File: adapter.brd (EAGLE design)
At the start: 75.9 x 17.8 mm, 3 parts

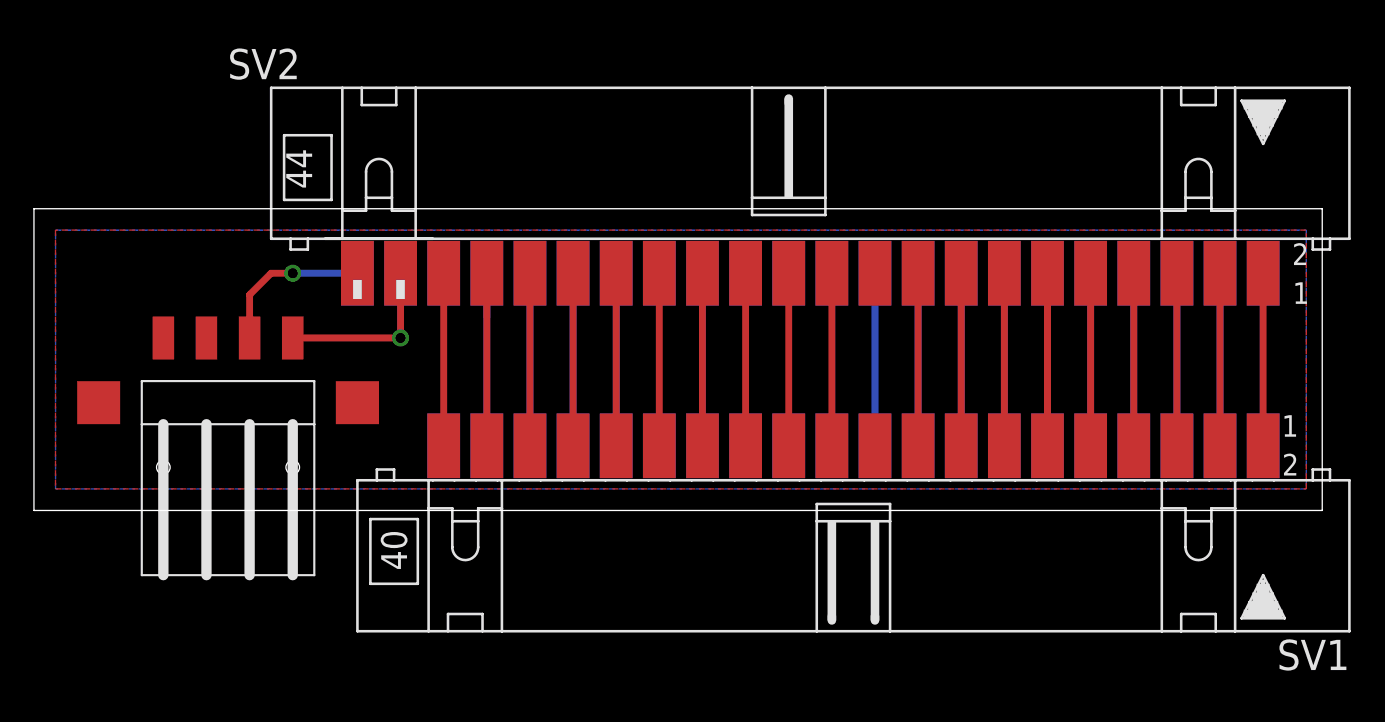
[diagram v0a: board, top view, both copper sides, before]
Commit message: Reduced pin pitch on the IDE 44 connector.
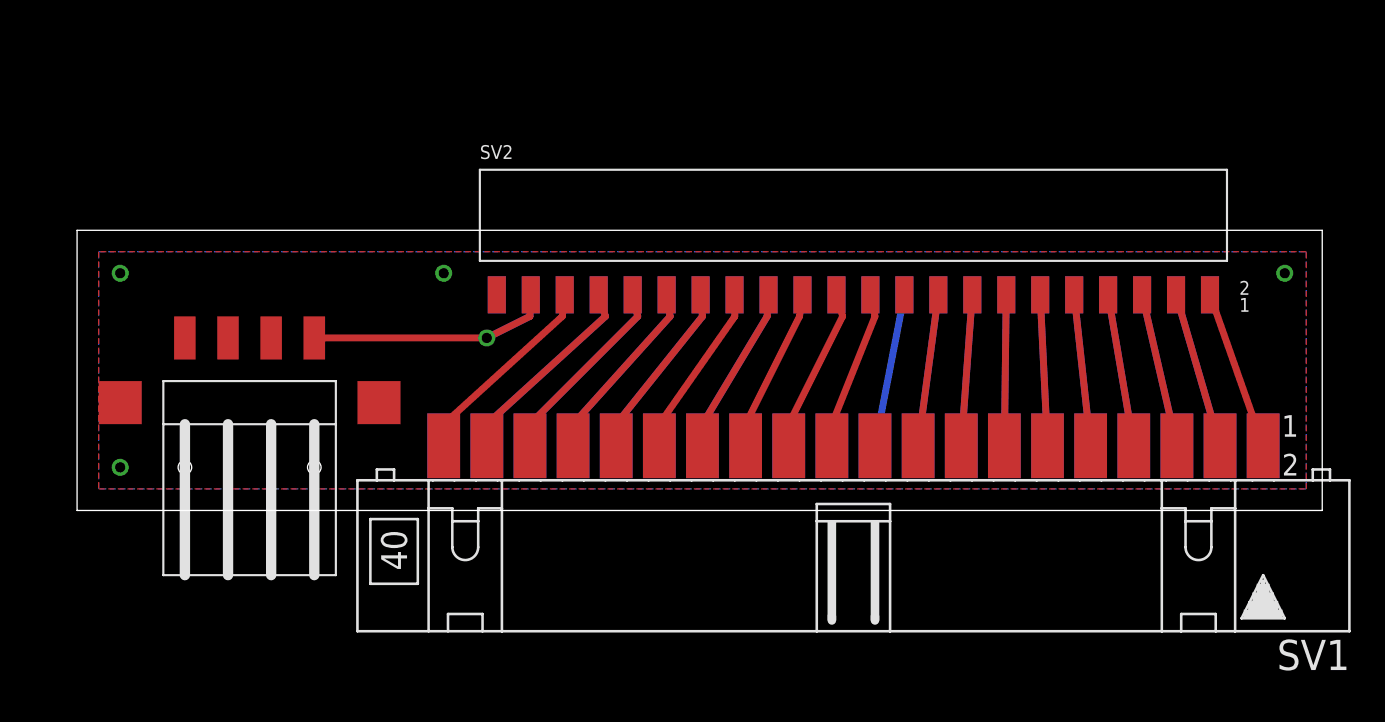
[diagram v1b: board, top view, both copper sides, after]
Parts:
- SV2: device conn:ML44SMDF -> conn:PINHEAD2X22F
- moved SV2 4.02 mm to (47.0, 11.4)
- moved U$1 1.27 mm to (11.4, 8.89)
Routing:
- net GND: track 9.42 -> 0.00 mm, vias 1 -> 4
- net N$3: track 14.0 -> 18.4 mm
- net IDE37: track 10.2 -> 12.0 mm
- net IDE39: track 10.2 -> 12.0 mm
- net IDE36: track 10.2 -> 11.6 mm
- net IDE35: track 10.2 -> 11.6 mm
- net IDE14: track 10.2 -> 8.89 mm
- net IDE13: track 10.2 -> 8.89 mm
- net IDE12: track 10.2 -> 8.90 mm
- net IDE11: track 10.2 -> 8.90 mm
- net IDE16: track 10.2 -> 8.91 mm
- net IDE15: track 10.2 -> 8.91 mm
- net IDE9: track 10.2 -> 8.94 mm
- net IDE10: track 10.2 -> 8.94 mm
- net IDE18: track 10.2 -> 8.97 mm
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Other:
- board size 75.9 x 17.8 mm -> 73.3 x 16.5 mm

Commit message: Added more space for the power plug.
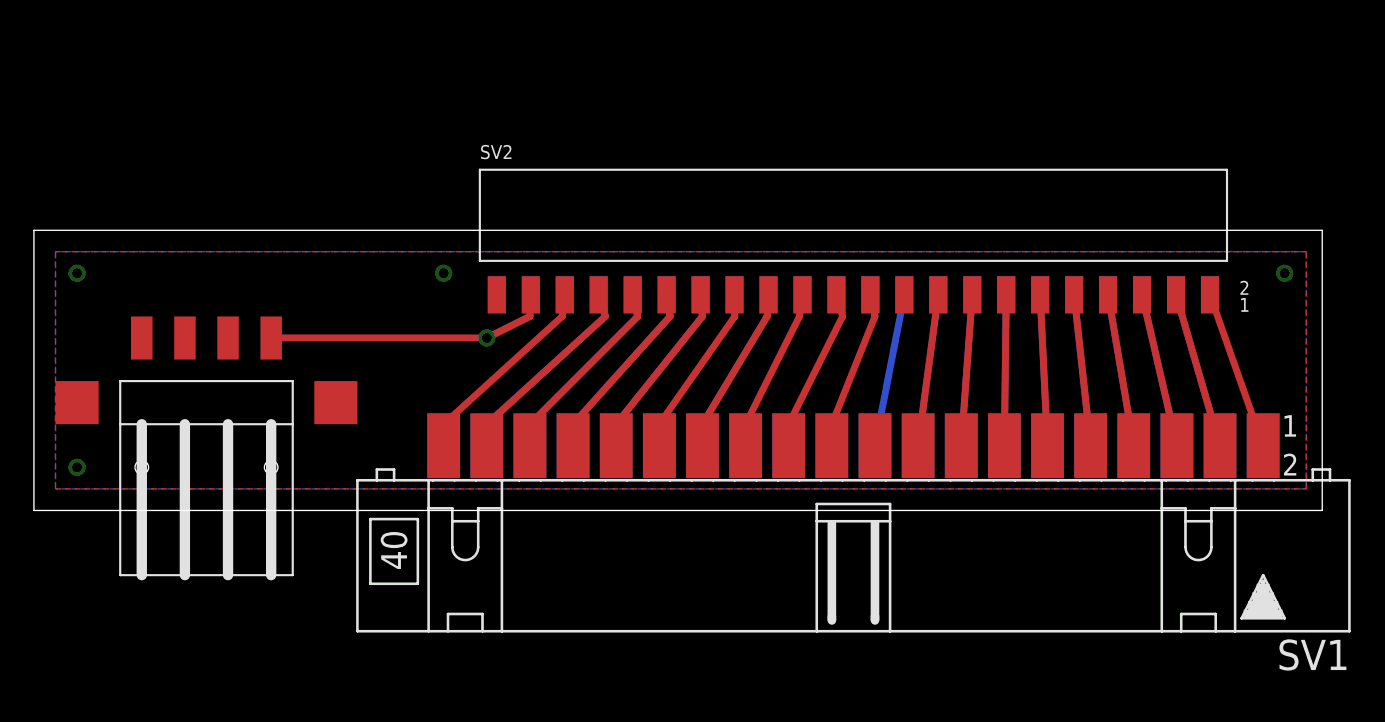
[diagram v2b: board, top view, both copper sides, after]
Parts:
- moved U$1 2.54 mm to (8.89, 8.89)
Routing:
- net N$3: track 18.4 -> 20.9 mm
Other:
- board size 73.3 x 16.5 mm -> 75.9 x 16.5 mm
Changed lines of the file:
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@@
 <board>
 <plain>
-<wire x1="1.27" y1="-1.27" x2="74.6" y2="-1.27" width="0" layer="20"/>
+<wire x1="-1.27" y1="-1.27" x2="74.6" y2="-1.27" width="0" layer="20"/>
 <wire x1="74.6" y1="-1.27" x2="74.6" y2="15.23" width="0" layer="20"/>
-<wire x1="74.6" y1="15.23" x2="1.27" y2="15.23" width="0" layer="20"/>
-<wire x1="1.27" y1="15.23" x2="1.27" y2="-1.27" width="0" layer="20"/>
+<wire x1="74.6" y1="15.23" x2="-1.27" y2="15.23" width="0" layer="20"/>
+<wire x1="-1.27" y1="15.23" x2="-1.27" y2="-1.27" width="0" layer="20"/>
 </plain>
 <attributes>
@@
 <element name="SV1" library="conn" package="ML40SMD" value="" x="46.99" y="2.54" rot="R180"/>
 <element name="SV2" library="conn" package="PINHEAD2X22F" value="" x="46.99" y="11.43"/>
-<element name="U$1" library="conn" package="FLOPPYPWR" value="FLOPPYPWR" x="11.43" y="8.89" rot="R180"/>
+<element name="U$1" library="conn" package="FLOPPYPWR" value="FLOPPYPWR" x="8.89" y="8.89" rot="R180"/>
 </elements>
 <signals>
@@
 <wire x1="27.94" y1="10.16" x2="25.4" y2="8.89" width="0.4064" layer="16"/>
 <via x="25.4" y="8.89" extent="1-16" drill="0.6" shape="square"/>
-<wire x1="25.4" y1="8.89" x2="15.24" y2="8.89" width="0.4064" layer="1"/>
+<wire x1="25.4" y1="8.89" x2="12.7" y2="8.89" width="0.4064" layer="1"/>
 </signal>
 <signal name="GND">
 <polygon width="0.4064" layer="1">
-<vertex x="2.54" y="0"/>
+<vertex x="0" y="0"/>
 <vertex x="73.66" y="0"/>
 <vertex x="73.66" y="13.97"/>
-<vertex x="2.54" y="13.97"/>
+<vertex x="0" y="13.97"/>
 </polygon>
 <polygon width="0.4064" layer="16">
-<vertex x="2.54" y="13.97"/>
+<vertex x="0" y="13.97"/>
 <vertex x="73.66" y="13.97"/>
 <vertex x="73.66" y="0"/>
-<vertex x="2.54" y="0"/>
+<vertex x="0" y="0"/>
 </polygon>
 <contactref element="U$1" pad="2"/>
@@
 <contactref element="SV1" pad="2"/>
 <contactref element="SV1" pad="19"/>
-<via x="3.81" y="12.7" extent="1-16" drill="0.6" shape="square"/>
+<via x="1.27" y="12.7" extent="1-16" drill="0.6" shape="square"/>
 <via x="22.86" y="12.7" extent="1-16" drill="0.6" shape="square"/>
-<via x="3.81" y="1.27" extent="1-16" drill="0.6" shape="square"/>
+<via x="1.27" y="1.27" extent="1-16" drill="0.6" shape="square"/>
 <via x="72.39" y="12.7" extent="1-16" drill="0.6" shape="square"/>
 </signal>

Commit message: Improved the PCB layout a little.
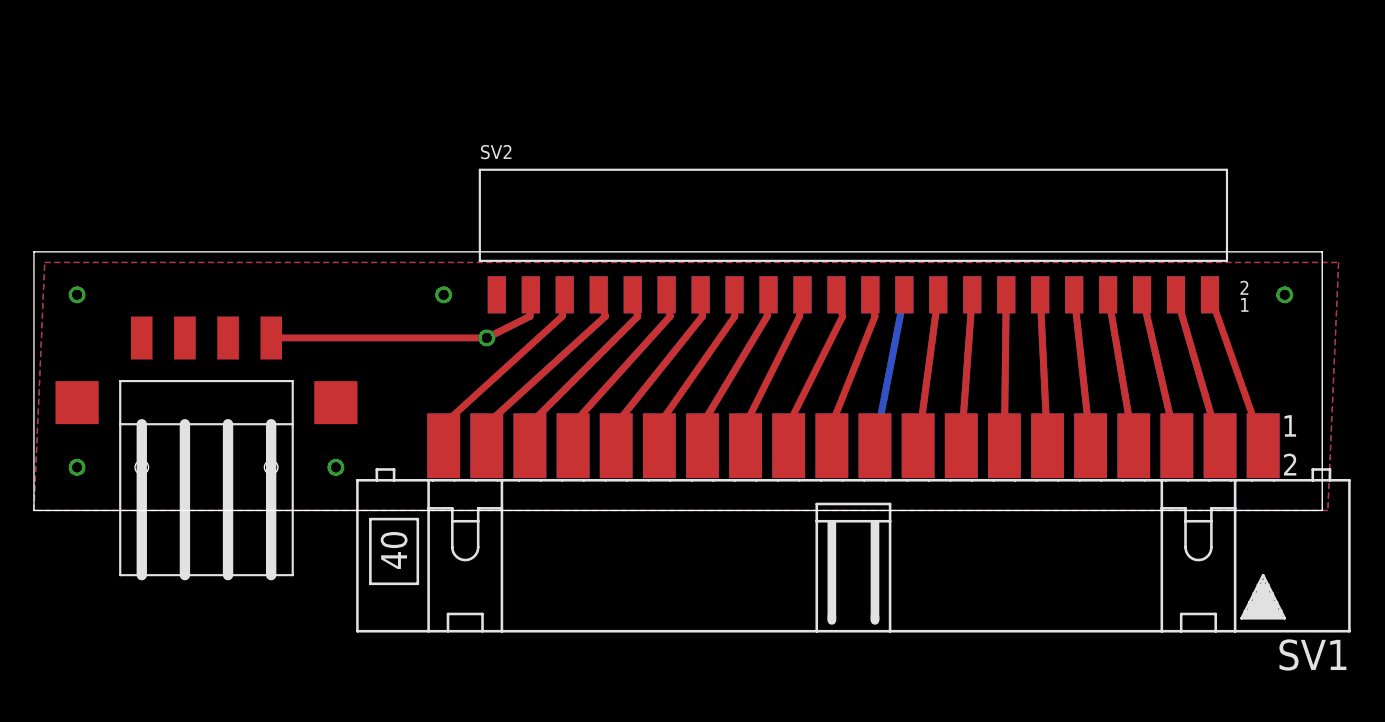
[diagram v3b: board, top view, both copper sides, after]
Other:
- board size 75.9 x 16.5 mm -> 75.9 x 15.2 mm
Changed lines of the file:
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@@
 <layer number="27" name="tValues" color="7" fill="1" visible="yes" active="yes"/>
 <layer number="28" name="bValues" color="7" fill="1" visible="yes" active="yes"/>
-<layer number="29" name="tStop" color="7" fill="3" visible="no" active="yes"/>
-<layer number="30" name="bStop" color="7" fill="6" visible="no" active="yes"/>
-<layer number="31" name="tCream" color="7" fill="4" visible="no" active="yes"/>
-<layer number="32" name="bCream" color="7" fill="5" visible="no" active="yes"/>
-<layer number="33" name="tFinish" color="6" fill="3" visible="no" active="yes"/>
-<layer number="34" name="bFinish" color="6" fill="6" visible="no" active="yes"/>
-<layer number="35" name="tGlue" color="7" fill="4" visible="no" active="yes"/>
-<layer number="36" name="bGlue" color="7" fill="5" visible="no" active="yes"/>
-<layer number="37" name="tTest" color="7" fill="1" visible="no" active="yes"/>
-<layer number="38" name="bTest" color="7" fill="1" visible="no" active="yes"/>
+<layer number="29" name="tStop" color="7" fill="3" visible="yes" active="yes"/>
+<layer number="30" name="bStop" color="7" fill="6" visible="yes" active="yes"/>
+<layer number="31" name="tCream" color="7" fill="4" visible="yes" active="yes"/>
+<layer number="32" name="bCream" color="7" fill="5" visible="yes" active="yes"/>
+<layer number="33" name="tFinish" color="6" fill="3" visible="yes" active="yes"/>
+<layer number="34" name="bFinish" color="6" fill="6" visible="yes" active="yes"/>
+<layer number="35" name="tGlue" color="7" fill="4" visible="yes" active="yes"/>
+<layer number="36" name="bGlue" color="7" fill="5" visible="yes" active="yes"/>
+<layer number="37" name="tTest" color="7" fill="1" visible="yes" active="yes"/>
+<layer number="38" name="bTest" color="7" fill="1" visible="yes" active="yes"/>
 <layer number="39" name="tKeepout" color="4" fill="11" visible="yes" active="yes"/>
 <layer number="40" name="bKeepout" color="1" fill="11" visible="yes" active="yes"/>
@@
 <layer number="42" name="bRestrict" color="1" fill="10" visible="yes" active="yes"/>
 <layer number="43" name="vRestrict" color="2" fill="10" visible="yes" active="yes"/>
-<layer number="44" name="Drills" color="7" fill="1" visible="no" active="yes"/>
-<layer number="45" name="Holes" color="7" fill="1" visible="no" active="yes"/>
-<layer number="46" name="Milling" color="3" fill="1" visible="no" active="yes"/>
-<layer number="47" name="Measures" color="7" fill="1" visible="no" active="yes"/>
+<layer number="44" name="Drills" color="7" fill="1" visible="yes" active="yes"/>
+<layer number="45" name="Holes" color="7" fill="1" visible="yes" active="yes"/>
+<layer number="46" name="Milling" color="3" fill="1" visible="yes" active="yes"/>
+<layer number="47" name="Measures" color="7" fill="1" visible="yes" active="yes"/>
 <layer number="48" name="Document" color="7" fill="1" visible="yes" active="yes"/>
 <layer number="49" name="Reference" color="7" fill="1" visible="yes" active="yes"/>
@@
 <plain>
 <wire x1="-1.27" y1="-1.27" x2="74.6" y2="-1.27" width="0" layer="20"/>
-<wire x1="74.6" y1="-1.27" x2="74.6" y2="15.23" width="0" layer="20"/>
-<wire x1="74.6" y1="15.23" x2="-1.27" y2="15.23" width="0" layer="20"/>
-<wire x1="-1.27" y1="15.23" x2="-1.27" y2="-1.27" width="0" layer="20"/>
+<wire x1="74.6" y1="-1.27" x2="74.6" y2="13.96" width="0" layer="20"/>
+<wire x1="74.6" y1="13.96" x2="-1.27" y2="13.96" width="0" layer="20"/>
+<wire x1="-1.27" y1="13.96" x2="-1.27" y2="-1.27" width="0" layer="20"/>
 </plain>
 <attributes>
@@
 </signal>
 <signal name="GND">
-<polygon width="0.4064" layer="1">
-<vertex x="0" y="0"/>
-<vertex x="73.66" y="0"/>
-<vertex x="73.66" y="13.97"/>
-<vertex x="0" y="13.97"/>
-</polygon>
-<polygon width="0.4064" layer="16">
-<vertex x="0" y="13.97"/>
-<vertex x="73.66" y="13.97"/>
-<vertex x="73.66" y="0"/>
-<vertex x="0" y="0"/>
-</polygon>
 <contactref element="U$1" pad="2"/>
 <contactref element="U$1" pad="3"/>
@@
 <contactref element="SV1" pad="2"/>
 <contactref element="SV1" pad="19"/>
-<via x="1.27" y="12.7" extent="1-16" drill="0.6" shape="square"/>
-<via x="22.86" y="12.7" extent="1-16" drill="0.6" shape="square"/>
+<via x="1.27" y="11.43" extent="1-16" drill="0.6" shape="square"/>
+<via x="22.86" y="11.43" extent="1-16" drill="0.6" shape="square"/>
 <via x="1.27" y="1.27" extent="1-16" drill="0.6" shape="square"/>
-<via x="72.39" y="12.7" extent="1-16" drill="0.6" shape="square"/>
+<via x="72.39" y="11.43" extent="1-16" drill="0.6" shape="square"/>
+<polygon width="0.4064" layer="16" isolate="0.254" orphans="yes">
+<vertex x="-0.635" y="13.335"/>
+<vertex x="75.565" y="13.335"/>
+<vertex x="74.93" y="-1.27"/>
+<vertex x="-1.27" y="-1.27"/>
+</polygon>
+<polygon width="0.4064" layer="1" isolate="0.254" orphans="yes">
+<vertex x="-0.635" y="13.335"/>
+<vertex x="75.565" y="13.335"/>
+<vertex x="74.93" y="-1.27"/>
+<vertex x="-1.27" y="-1.27"/>
+</polygon>
+</signal>
+<signal name="S$1">
+<via x="16.51" y="1.27" extent="1-16" drill="0.6" diameter="0.6096" shape="square"/>
 </signal>
 </signals>

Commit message: Adjusted the board layout.
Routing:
- net N$3: track 20.9 -> 24.7 mm
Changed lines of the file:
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@@
 <contactref element="SV2" pad="42"/>
 <contactref element="SV2" pad="41"/>
-<wire x1="25.4" y1="8.89" x2="27.94" y2="10.16" width="0.4064" layer="1"/>
-<wire x1="27.94" y1="10.16" x2="27.99" y2="11.43" width="0.4064" layer="1"/>
+<wire x1="22.86" y1="8.255" x2="26.035" y2="8.255" width="0.4064" layer="1"/>
+<wire x1="26.035" y1="8.255" x2="27.94" y2="10.16" width="0.4064" layer="1"/>
+<wire x1="27.94" y1="10.16" x2="27.94" y2="11.38" width="0.4064" layer="1"/>
+<wire x1="27.94" y1="11.38" x2="27.99" y2="11.43" width="0.4064" layer="1"/>
 <wire x1="27.99" y1="11.43" x2="27.94" y2="10.16" width="0.4064" layer="16"/>
-<wire x1="27.94" y1="10.16" x2="25.4" y2="8.89" width="0.4064" layer="16"/>
-<via x="25.4" y="8.89" extent="1-16" drill="0.6" shape="square"/>
-<wire x1="25.4" y1="8.89" x2="12.7" y2="8.89" width="0.4064" layer="1"/>
+<wire x1="27.94" y1="10.16" x2="26.035" y2="8.255" width="0.4064" layer="16"/>
+<wire x1="26.035" y1="8.255" x2="22.86" y2="8.255" width="0.4064" layer="16"/>
+<via x="22.86" y="8.255" extent="1-16" drill="0.8" shape="square"/>
+<wire x1="22.86" y1="8.255" x2="13.335" y2="8.255" width="0.4064" layer="1"/>
+<wire x1="13.335" y1="8.255" x2="12.7" y2="8.89" width="0.4064" layer="1"/>
 </signal>
 <signal name="GND">
@@
 <contactref element="SV1" pad="2"/>
 <contactref element="SV1" pad="19"/>
-<via x="1.27" y="11.43" extent="1-16" drill="0.6" shape="square"/>
-<via x="22.86" y="11.43" extent="1-16" drill="0.6" shape="square"/>
-<via x="1.27" y="1.27" extent="1-16" drill="0.6" shape="square"/>
-<via x="72.39" y="11.43" extent="1-16" drill="0.6" shape="square"/>
-<polygon width="0.4064" layer="16" isolate="0.254" orphans="yes">
-<vertex x="-0.635" y="13.335"/>
-<vertex x="75.565" y="13.335"/>
-<vertex x="74.93" y="-1.27"/>
-<vertex x="-1.27" y="-1.27"/>
+<via x="1.27" y="11.43" extent="1-16" drill="0.8" shape="square"/>
+<via x="22.86" y="11.43" extent="1-16" drill="0.8" shape="square"/>
+<via x="1.27" y="1.27" extent="1-16" drill="0.8" shape="square"/>
+<via x="72.39" y="11.43" extent="1-16" drill="0.8" shape="square"/>
+<polygon width="0.4064" layer="16" isolate="0.4064" orphans="yes">
+<vertex x="0" y="13.335"/>
+<vertex x="73.66" y="13.335"/>
+<vertex x="73.66" y="0"/>
+<vertex x="0" y="0"/>
 </polygon>
-<polygon width="0.4064" layer="1" isolate="0.254" orphans="yes">
-<vertex x="-0.635" y="13.335"/>
-<vertex x="75.565" y="13.335"/>
-<vertex x="74.93" y="-1.27"/>
-<vertex x="-1.27" y="-1.27"/>
+<polygon width="0.4064" layer="1" isolate="0.4064" orphans="yes">
+<vertex x="0" y="13.335"/>
+<vertex x="73.66" y="13.335"/>
+<vertex x="73.66" y="0"/>
+<vertex x="0" y="0"/>
 </polygon>
-</signal>
-<signal name="S$1">
-<via x="16.51" y="1.27" extent="1-16" drill="0.6" diameter="0.6096" shape="square"/>
+<via x="16.51" y="1.27" extent="1-16" drill="0.8" diameter="0.6096" shape="square"/>
 </signal>
 </signals>
